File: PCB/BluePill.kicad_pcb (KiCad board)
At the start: 2 copper layers, 53.3 x 22.9 mm, 36 parts, among them J1 USB_B_Micro, J2 Conn_01x20, J3 Conn_02x03_Odd_Even, J4 Conn_01x20, J5 Conn_01x04, SW1 SW_Push, U1 STM32F103C8Tx, U2 RT9193-33, Y1 Crystal_GND24_Small, Y2 8MHZ

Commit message: 微调
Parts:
- moved C1 0.76 mm to (116.3, 90.2)
- moved J5 0.69 mm to (114.0, 86.4)
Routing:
- net GND: track 141.3 -> 137.4 mm, vias 9 -> 13
- net /PC14: track 38.5 -> 35.8 mm
- net +3V3: track 105.5 -> 103.2 mm
- net Net-(J1-Pad3): track 18.5 -> 19.4 mm
- net /SWDCLK: track 26.5 -> 25.7 mm
- net /SWDIO: track 29.7 -> 29.0 mm
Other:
- board text added: "CLK"
- board text added: "DIO"
- board text added: "GND"
- board text added: "RST"
- board text removed: "G"
- board text removed: "R"

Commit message: 更换USB插座封装
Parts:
- J1: footprint Connector_USB:USB_Micro-B_Molex_47346-0001 -> Connector_USB:USB_Micro-B_Molex-105017-0001
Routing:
- net GND: track 137.4 -> 136.2 mm

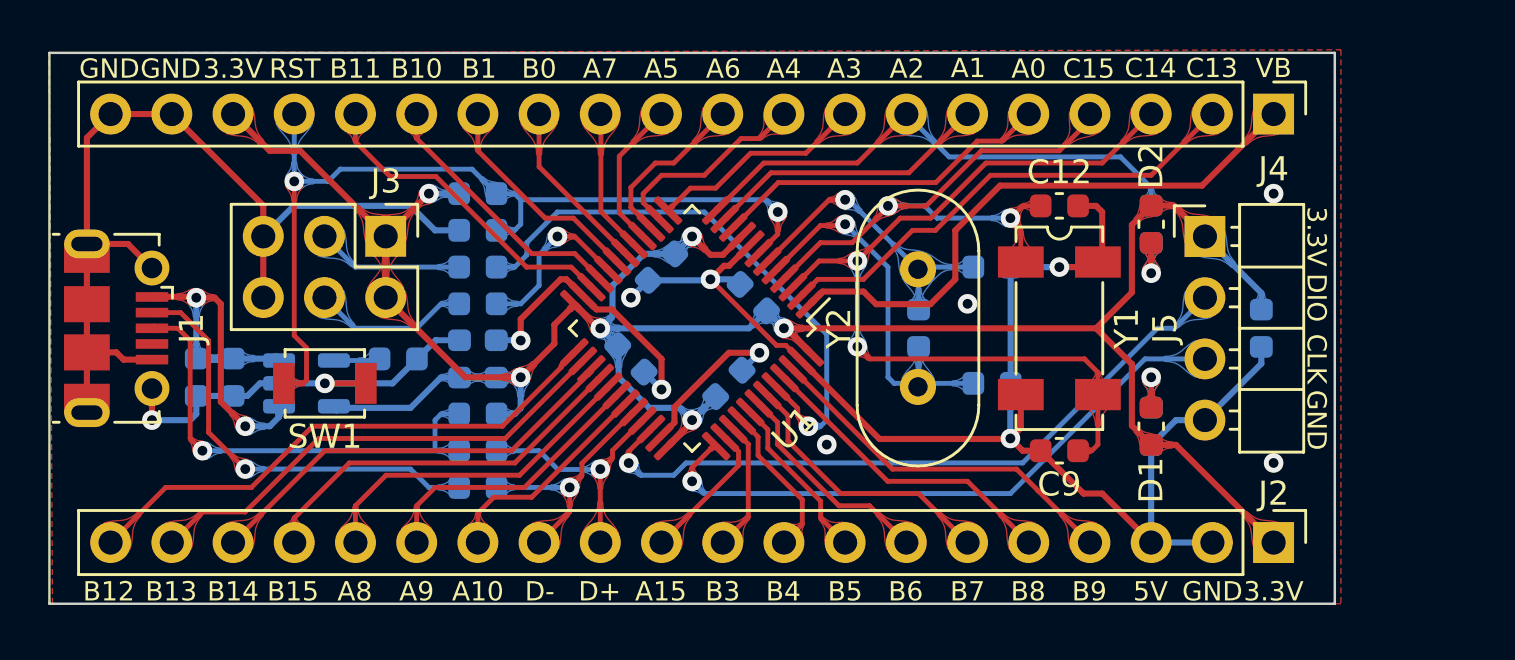
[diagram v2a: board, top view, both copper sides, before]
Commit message: 修复32K晶振问题；局部优化。
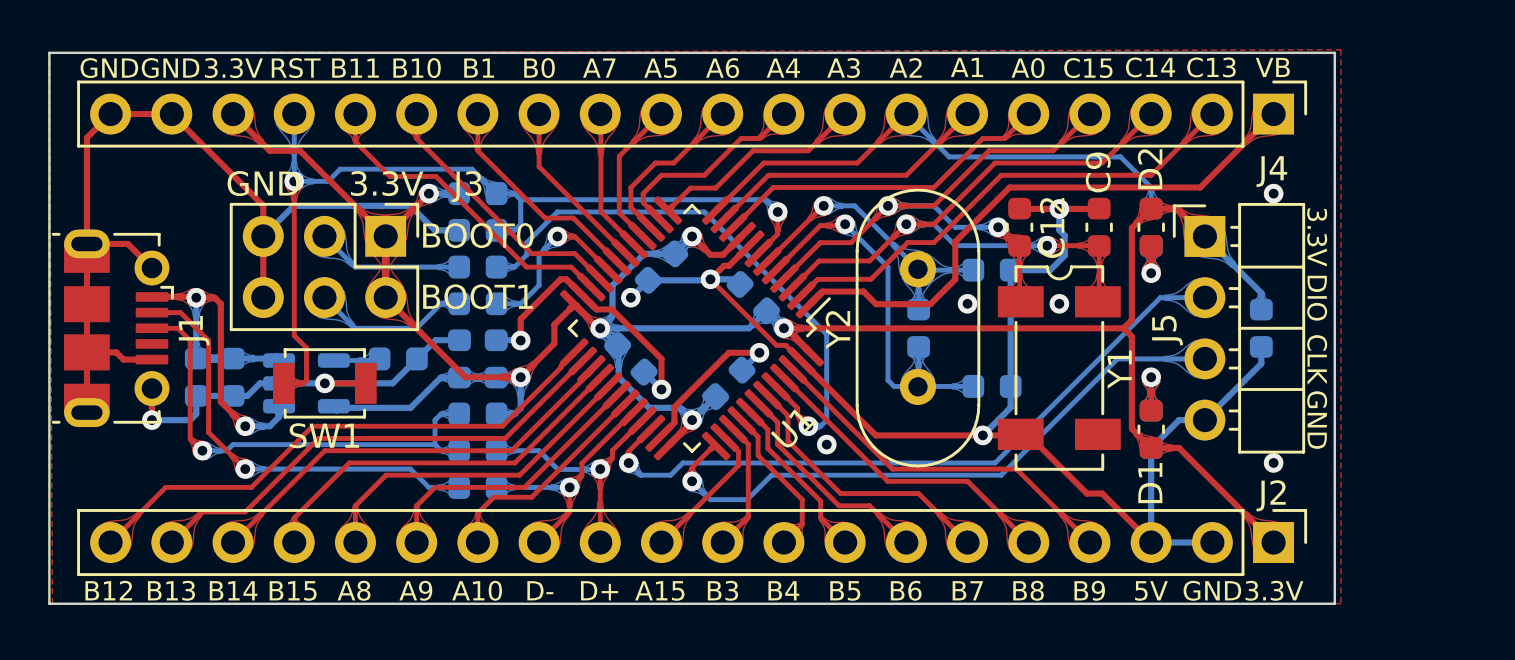
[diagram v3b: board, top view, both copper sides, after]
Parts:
- moved C9 9.42 mm to (109.6, 86.0), turned to -90 degrees
- moved C12 1.88 mm to (106.3, 86.0), turned to 90 degrees
- moved Y1 1.65 mm to (108.0, 91.8)
- moved C14 0.13 mm to (105.2, 87.8)
- moved D1 0.13 mm to (111.8, 94.4)
- moved R1 0.13 mm to (111.8, 94.4)
- moved C13 0.13 mm to (105.2, 92.6)
- moved D2 0.13 mm to (111.8, 86.0)
- moved R5 0.13 mm to (111.8, 86.0)
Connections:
- Y1 pad 3: /PC14 -> GND
- Y1 pad 4: GND -> /PC14
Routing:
- net /PC14: track 35.8 -> 28.6 mm
- net GND: track 136.2 -> 134.9 mm, vias 13 -> 14
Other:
- board text added: "BOOT0"
- board text added: "BOOT1"
